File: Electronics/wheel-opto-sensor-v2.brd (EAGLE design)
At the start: 31.1 x 16.5 mm, 9 parts

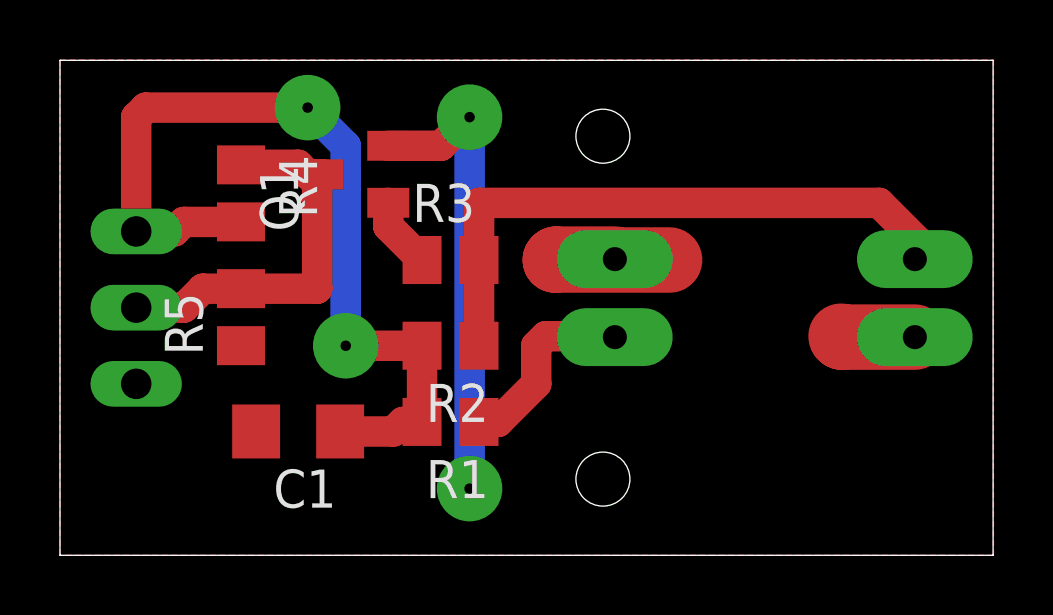
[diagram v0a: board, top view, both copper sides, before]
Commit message: Added LED to shield, and anti-short safety diode to the charge circuit.
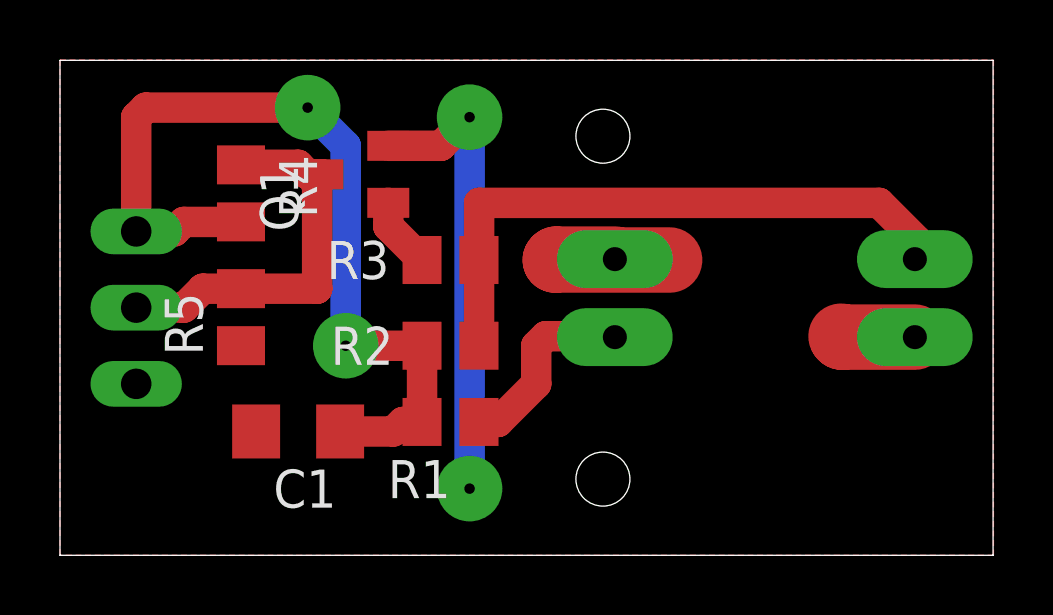
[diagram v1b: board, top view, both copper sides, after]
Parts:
- R2: value 1K8 -> 4K7
- R4: value 1K2 -> 6K8
- R5: value 1K -> 4K7
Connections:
- net +3V3 renamed +6V5
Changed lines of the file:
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@@
 <element name="C1" library="rcl" package="C1206" value="10uF" x="7.9375" y="4.1275" rot="R180"/>
 <element name="Q1" library="adafruit" package="SOT23" value="" x="9.8425" y="12.7" rot="R90"/>
-<element name="R1" library="rcl" package="M0805" value="120R" x="13.0175" y="4.445" rot="R180"/>
-<element name="R2" library="rcl" package="M0805" value="1K8" x="13.0175" y="6.985" rot="R180"/>
-<element name="R3" library="rcl" package="M0805" value="10K" x="13.0175" y="9.8425"/>
-<element name="R4" library="rcl" package="M0805" value="1K2" x="6.0325" y="12.065" rot="R270"/>
+<element name="R1" library="rcl" package="M0805" value="120R" x="13.0175" y="4.445" smashed="yes" rot="R180">
+<attribute name="NAME" x="13.0175" y="3.175" size="1.27" layer="25" rot="R180"/>
+<attribute name="VALUE" x="19.05" y="5.08" size="1.27" layer="27" rot="R180"/>
+</element>
+<element name="R2" library="rcl" package="M0805" value="4K7" x="13.0175" y="6.985" smashed="yes" rot="R180">
+<attribute name="NAME" x="11.1125" y="7.62" size="1.27" layer="25" rot="R180"/>
+<attribute name="VALUE" x="17.78" y="7.3025" size="1.27" layer="27" rot="R180"/>
+</element>
+<element name="R3" library="rcl" package="M0805" value="10K" x="13.0175" y="9.8425" smashed="yes">
+<attribute name="NAME" x="8.89" y="9.2075" size="1.27" layer="25"/>
+<attribute name="VALUE" x="14.605" y="9.2075" size="1.27" layer="27"/>
+</element>
+<element name="R4" library="rcl" package="M0805" value="6K8" x="6.0325" y="12.065" rot="R270"/>
 <element name="JP1" library="pinhead" package="1X03" value="" x="2.54" y="8.255" rot="MR270"/>
-<element name="R5" library="rcl" package="M0805" value="1K" x="6.0325" y="7.9375" rot="R90"/>
+<element name="R5" library="rcl" package="M0805" value="4K7" x="6.0325" y="7.9375" rot="R90"/>
 <element name="U$1" library="reprapltd" package="RPI-579N1" value="RPI-579N1" x="23.495" y="8.5725" rot="MR180"/>
 </elements>
@@
 <wire x1="28.575" y1="9.9525" x2="28.495" y2="9.8725" width="1.016" layer="1"/>
 </signal>
-<signal name="+3V3">
+<signal name="+6V5">
 <contactref element="R2" pad="2"/>
 <contactref element="R4" pad="2"/>

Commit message: PCBs corrected (D9 now LED) and improved (wheel sensor has 4 mounting holes); software updated to match.
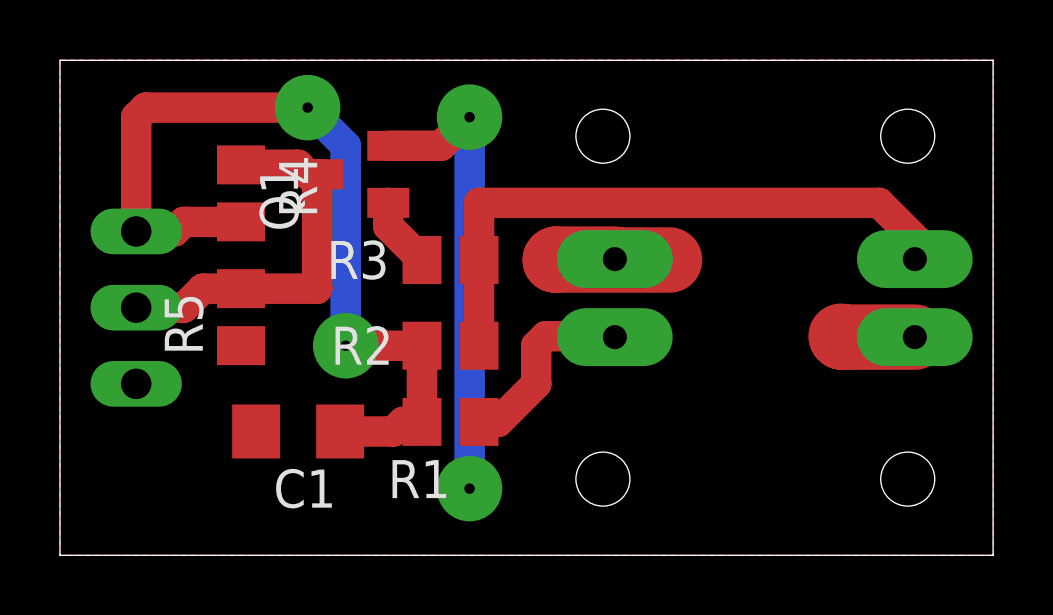
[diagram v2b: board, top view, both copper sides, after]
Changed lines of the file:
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@@
 <?xml version="1.0" encoding="utf-8"?>
 <!DOCTYPE eagle SYSTEM "eagle.dtd">
-<eagle version="7.5.0">
+<eagle version="8.2.1">
 <drawing>
 <settings>
@@
 <hole x="18.0975" y="2.54" drill="1.8"/>
 <hole x="18.0975" y="13.97" drill="1.8"/>
+<hole x="28.2575" y="13.97" drill="1.8"/>
+<hole x="28.2575" y="2.54" drill="1.8"/>
 </plain>
 <attributes>
